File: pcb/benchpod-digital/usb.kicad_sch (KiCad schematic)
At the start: 31 parts, among them U35 INA226, U57 TPS259470ARPWR

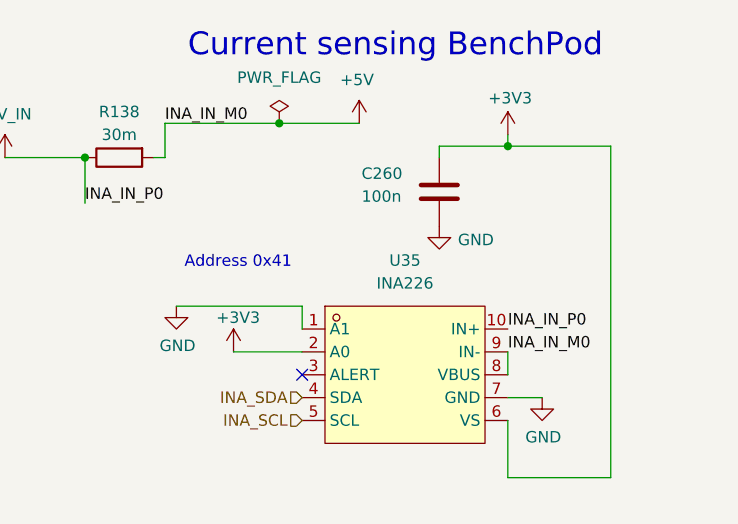
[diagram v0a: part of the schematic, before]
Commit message: digital: U35 value INA226AIDGSR like U29/U33
With two different values the JLC BOM had two lines for the same part
(C49851) and left both unconfirmed at quantity 0, so no INA226 would have
been placed. One value gives one line, U29/U33/U35.

Co-Authored-By: Claude Opus 5.5 <noreply@anthropic.com>
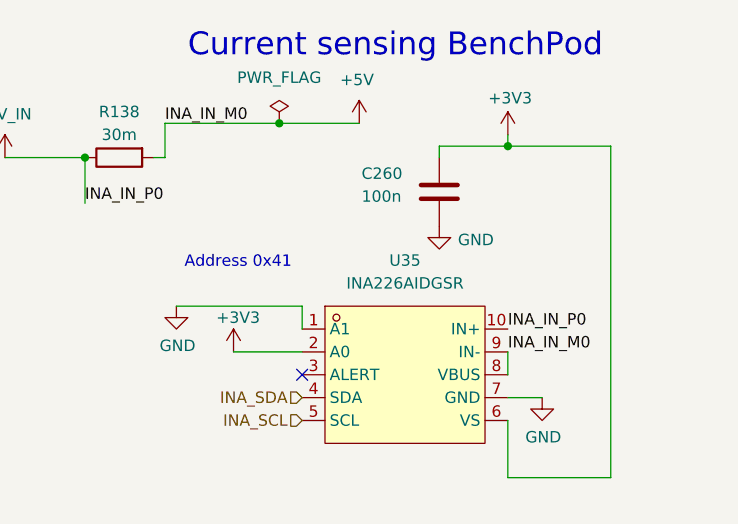
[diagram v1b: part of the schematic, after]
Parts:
- U35: value INA226 -> INA226AIDGSR
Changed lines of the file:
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@@
 			)
 		)
-		(property "Value" "INA226"
+		(property "Value" "INA226AIDGSR"
 			(at 247.65 129.54 0)
 			(show_name no)

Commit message: digital v3r3: carry over the analog v3r2 schematic changes
Same refs and nets as analog v3r1 in these areas, so the v3r2 fixes map 1:1.

- RoHS: D3 SS34 C8678 -> C3014011, D5 SMAJ20A C41376408 -> C5353170.
- U4 ESP32-C3-MINI-1-H4 (C2934569): the N4 is out of stock at JLC; same
  module, footprint and chip, 105 C rated.
- Package shrinks (whole BOM lines, no new lines): 8.2p C29/C30/C50/C51 and
  3.3n C99/C102/C119/C226 0603 -> 0402, 2.2u C218/C219 1206 -> 0603.
- EMC: D11 spare channels on USB CC1/CC2, U34 spares on +1V8 and LA_VCCIO.
- Debug: H1 (SWD 2x5) and H3 (HEADER1) removed; J10 SWO/NRST/SWCLK/SWDIO and
  J11 USART2_RX/+3V3/GND/USART2_TX 2x2, both DNP; PB3 = SWO, PD5/PD6 = USART2.

Not carried over: the 0.1 % resistors (on analog they only share lines with
the ADC parts) and the R164 revision strap (stays 1k: firmware runs the
digital board as v3). The PCB still needs Update PCB from Schematic.

Co-Authored-By: Claude Opus 5.5 <noreply@anthropic.com>
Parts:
- C226: footprint Capacitor_SMD:C_0603_1608Metric -> Capacitor_SMD:C_0402_1005Metric; LCSC C1613 -> C26404
- D3: LCSC C8678 -> C3014011; LCSC Part C8678 -> C3014011; Manufacturer MDD(辰达半导体) -> FOSAN
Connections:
- net USB_CC2: now reaches R179.1, R75.2, USBC1.B5 (CC2)
- net USB_CC2: now also D11.4
- net USB_CC1: now reaches D11.6
- net USB_CC1: now also R178.1, R76.1, USBC1.A5 (CC1)
- no-connect marks 5 -> 3
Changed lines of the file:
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@@
 	)
 	(no_connect
-		(at 162.56 59.69)
-	)
-	(no_connect
 		(at 236.22 139.7)
 	)
@@
 		(at 76.2 57.15)
 	)
-	(no_connect
-		(at 162.56 41.91)
-	)
 	(wire
 		(pts
@@
 		)
 	)
+	(label "USB_CC2"
+		(at 162.56 59.69 0)
+		(effects
+			(font
+				(size 1.27 1.27)
+			)
+			(justify left bottom)
+		)
+	)
+	(label "USB_CC1"
+		(at 76.2 44.45 180)
+		(effects
+			(font
+				(size 1.27 1.27)
+			)
+			(justify right bottom)
+		)
+	)
+	(label "USB_CC2"
+		(at 76.2 59.69 180)
+		(effects
+			(font
+				(size 1.27 1.27)
+			)
+			(justify right bottom)
+		)
+	)
+	(label "USB_CC1"
+		(at 162.56 41.91 0)
+		(effects
+			(font
+				(size 1.27 1.27)
+			)
+			(justify left bottom)
+		)
+	)
 	(label "5V_IN"
 		(at 60.96 39.37 180)
@@
 			)
 		)
-		(property "Manufacturer" "MDD(辰达半导体)"
+		(property "Manufacturer" "FOSAN"
 			(at 124.46 142.24 0)
 			(hide yes)
@@
 			)
 		)
-		(property "LCSC Part" "C8678"
+		(property "LCSC Part" "C3014011"
 			(at 119.38 142.24 0)
 			(hide yes)
@@
 			)
 		)
-		(property "LCSC" "C8678"
+		(property "LCSC" "C3014011"
 			(at 137.16 142.24 90)
 			(hide yes)
@@
 			)
 		)
-		(property "Footprint" "Capacitor_SMD:C_0603_1608Metric"
+		(property "Footprint" "Capacitor_SMD:C_0402_1005Metric"
 			(at 127.9652 101.6 0)
 			(hide yes)
@@
 			)
 		)
-		(property "LCSC" "C1613"
+		(property "LCSC" "C26404"
 			(at 127 97.79 0)
 			(hide yes)
